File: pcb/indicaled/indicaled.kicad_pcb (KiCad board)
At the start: 2 copper layers, 1 part

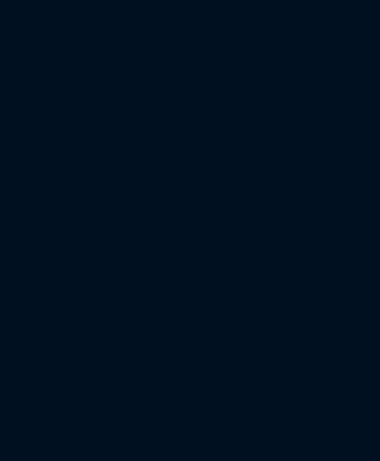
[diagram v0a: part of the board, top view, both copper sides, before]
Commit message: adicionando valores aos componentes
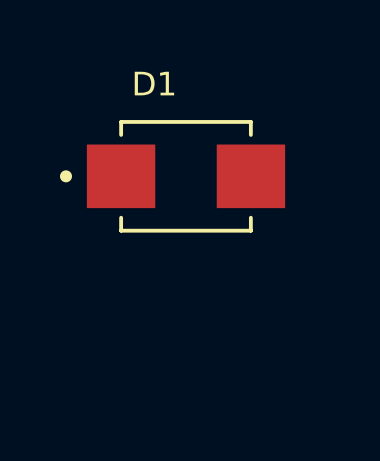
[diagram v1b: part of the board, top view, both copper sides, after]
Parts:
- added D1: D, ss26:SS26, F.Cu at (190.3, 110.2)
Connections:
- U1 pad 1: unconnected-(U1-BOOT-Pad1) -> Net-(U1-BOOT)
- U1 pad 2: unconnected-(U1-VIN-Pad2) -> VIN
- U1 pad 3: unconnected-(U1-EN-Pad3) -> Net-(U1-EN)
- U1 pad 4: unconnected-(U1-SS-Pad4) -> Net-(U1-SS)
- U1 pad 5: unconnected-(U1-VSENSE-Pad5) -> Net-(U1-VSENSE)
- U1 pad 6: unconnected-(U1-COMP-Pad6) -> Net-(U1-COMP)
- U1 pad 7: unconnected-(U1-GND-Pad7) -> GND
- U1 pad 8: unconnected-(U1-PH-Pad8) -> Net-(D1-K)

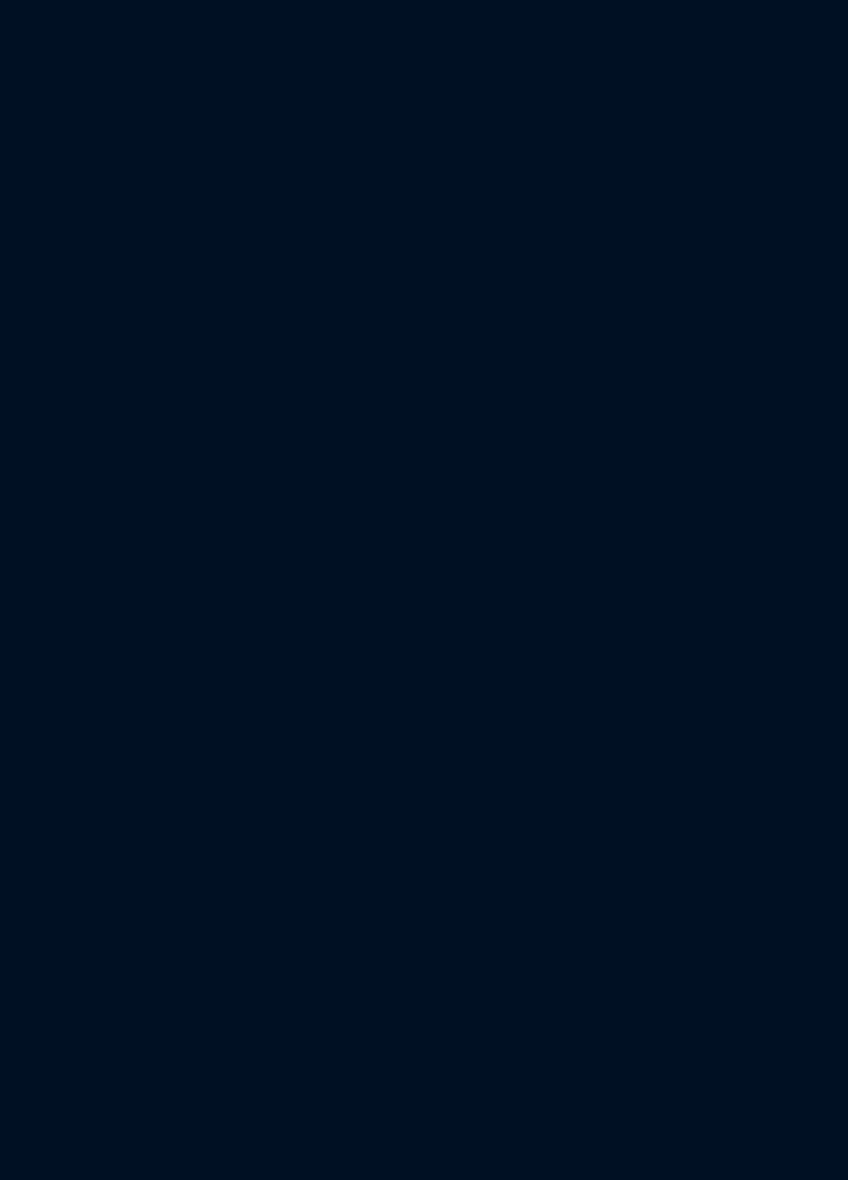
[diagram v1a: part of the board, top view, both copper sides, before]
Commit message: adicionando footprints aos componentes do circuito de alimentação
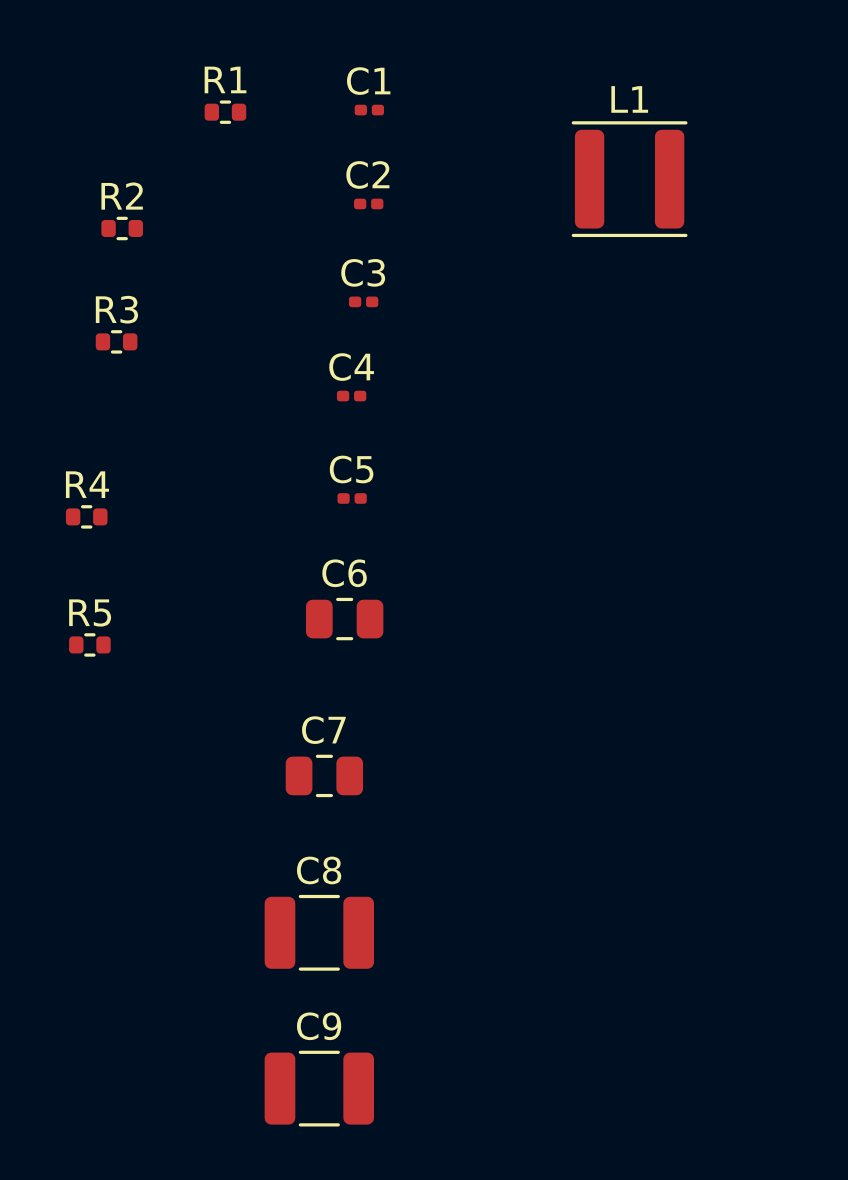
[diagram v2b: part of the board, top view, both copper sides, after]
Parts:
- added C1: 4.7nF, Capacitor_SMD:C_0201_0603Metric, F.Cu at (166.8, 105.1)
- added C2: 39pF, Capacitor_SMD:C_0201_0603Metric, F.Cu at (166.8, 108.6)
- added C3: .01uF, Capacitor_SMD:C_0201_0603Metric, F.Cu at (166.6, 112.3)
- added C4: .1uF, Capacitor_SMD:C_0201_0603Metric, F.Cu at (166.1, 115.8)
- added C5: .01uF, Capacitor_SMD:C_0201_0603Metric, F.Cu at (166.1, 119.7)
- added C6: 4700pF, Capacitor_SMD:C_0805_2012Metric, F.Cu at (165.8, 124.2)
- added C7: 39pF, Capacitor_SMD:C_0805_2012Metric, F.Cu at (165.1, 130.1)
- added C8: 33uF, Capacitor_SMD:C_1210_3225Metric, F.Cu at (164.9, 135.9)
- added C9: 33uF, Capacitor_SMD:C_1210_3225Metric, F.Cu at (164.9, 141.8)
- added L1: 6.8uH, Inductor_SMD:L_APV_ANR4020, F.Cu at (176.5, 107.7)
- added R1: 10k, Resistor_SMD:R_0402_1005Metric, F.Cu at (161.4, 105.2)
- added R2: 1.91k, Resistor_SMD:R_0402_1005Metric, F.Cu at (157.5, 109.5)
- added R3: 49.9k, Resistor_SMD:R_0402_1005Metric, F.Cu at (157.3, 113.8)
- added R4: 10k, Resistor_SMD:R_0402_1005Metric, F.Cu at (156.2, 120.3)
- added R5: 1.9k, Resistor_SMD:R_0402_1005Metric, F.Cu at (156.3, 125.1)

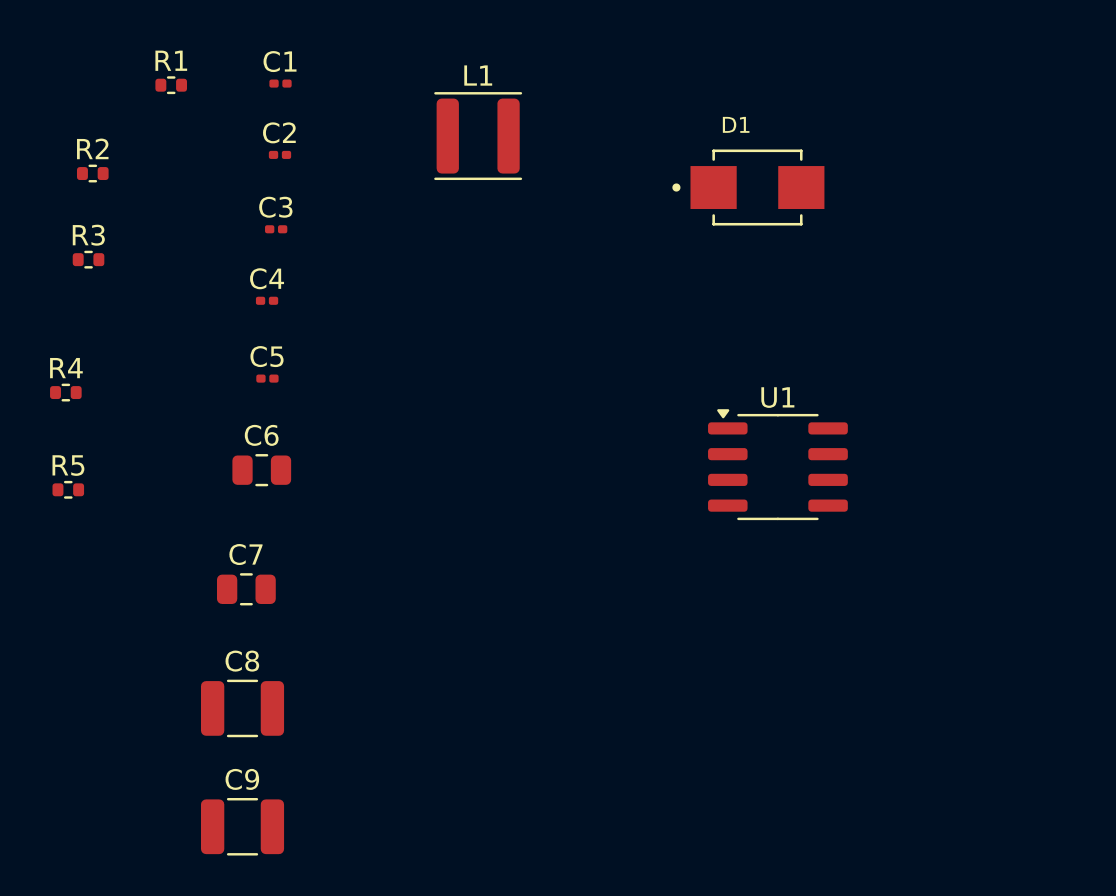
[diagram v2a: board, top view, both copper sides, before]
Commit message: fazendo as ligações do circuito de alimentação e mudando o footprint do D1
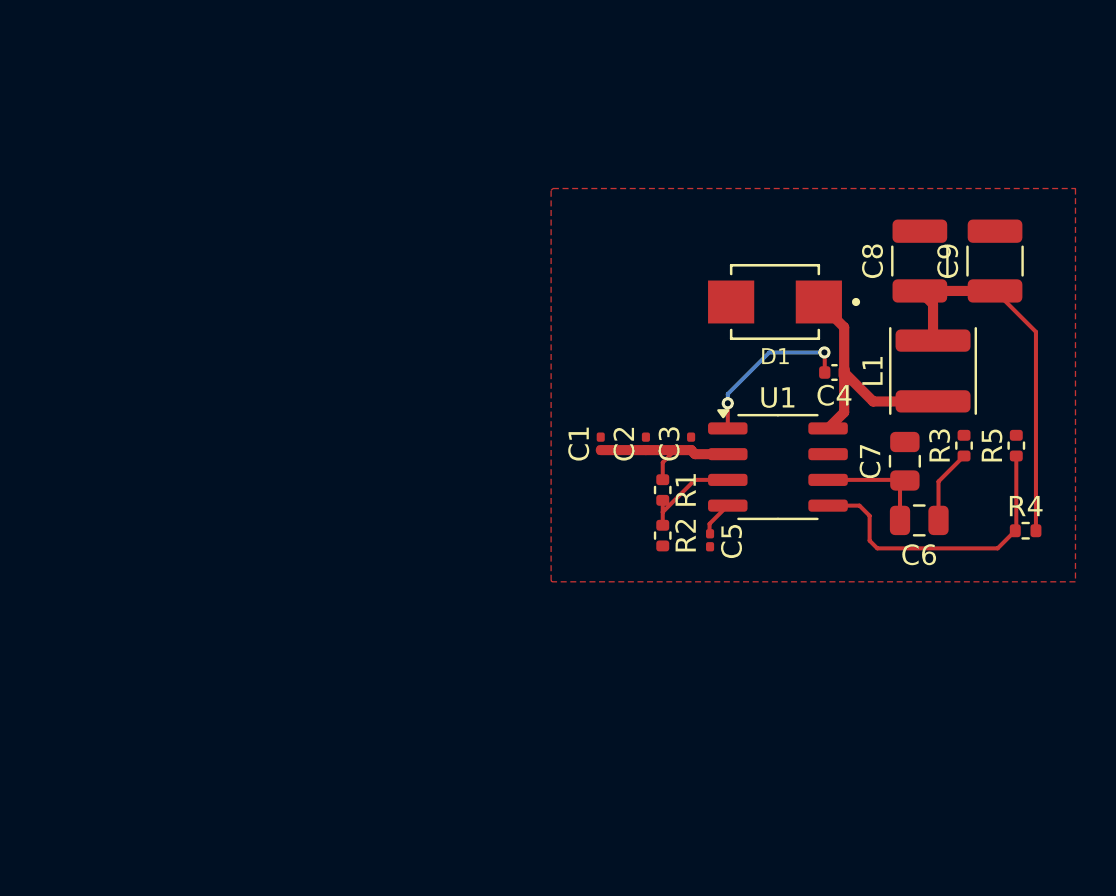
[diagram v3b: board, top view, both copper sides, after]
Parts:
- C4: footprint Capacitor_SMD:C_0201_0603Metric -> Capacitor_SMD:C_0402_1005Metric
- D1: value D -> SS26
- moved R4 47.9 mm to (203.6, 127.2), turned to 180 degrees
- moved R5 46.8 mm to (203.1, 123.0), turned to 90 degrees
- moved C9 46.5 mm to (202.0, 113.8), turned to 90 degrees
- moved R3 44.2 mm to (200.5, 123.0), turned to 90 degrees
- moved C8 40.1 mm to (198.3, 113.8), turned to 90 degrees
- moved R2 33.3 mm to (185.6, 127.4), turned to -90 degrees
- moved C7 33.1 mm to (197.6, 123.7), turned to 90 degrees
- moved C6 32.5 mm to (198.3, 126.7)
- moved R1 31.4 mm to (185.6, 125.2), turned to -90 degrees
- moved C4 28.2 mm to (194.1, 119.3), turned to 180 degrees
- moved L1 25.3 mm to (199.0, 119.3), turned to 90 degrees
- moved C1 23.8 mm to (182.6, 122.9), turned to 90 degrees
- moved C5 23.3 mm to (188.0, 127.6), turned to -90 degrees
- moved C3 23.1 mm to (187.0, 122.9), turned to 90 degrees
- moved C2 23.0 mm to (184.8, 122.9), turned to 90 degrees
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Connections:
- C4 pad 1: Net-(D1-K) -> Net-(U1-PH)
- L1 pad 1: Net-(D1-K) -> Net-(U1-PH)
- U1 pad 8: Net-(D1-K) -> Net-(U1-PH)
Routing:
- net VOUT: track 0.00 -> 19.1 mm
- net Net-(U1-VSENSE): track 0.00 -> 14.9 mm
- net Net-(U1-PH): track 0.00 -> 12.1 mm
- net Net-(U1-BOOT): track 0.00 -> 8.32 mm, vias 0 -> 2
- net VIN: track 0.00 -> 8.07 mm
- net Net-(U1-COMP): track 0.00 -> 5.87 mm
- net Net-(U1-EN): track 0.00 -> 5.10 mm
- net Net-(C6-Pad2): track 0.00 -> 3.70 mm
- net Net-(U1-SS): track 0.00 -> 1.87 mm
- added copper zone on F.Cu, net GND

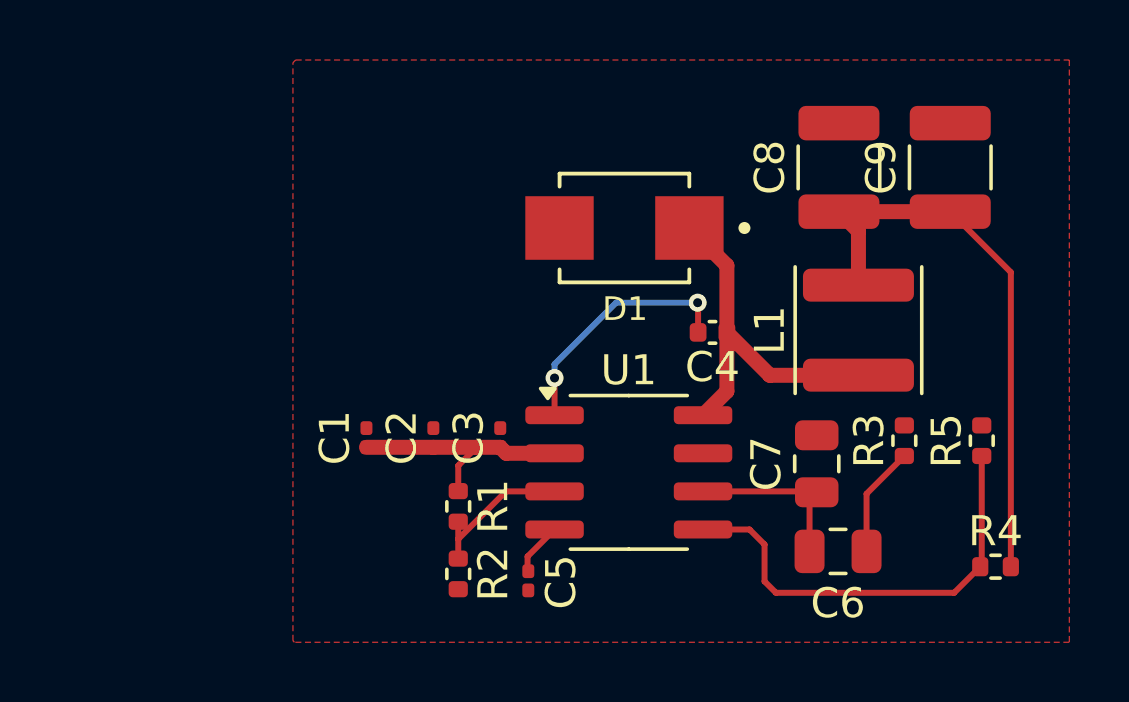
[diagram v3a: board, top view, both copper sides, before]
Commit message: trocando os capacitores de acoplamento de 0201 para 1210
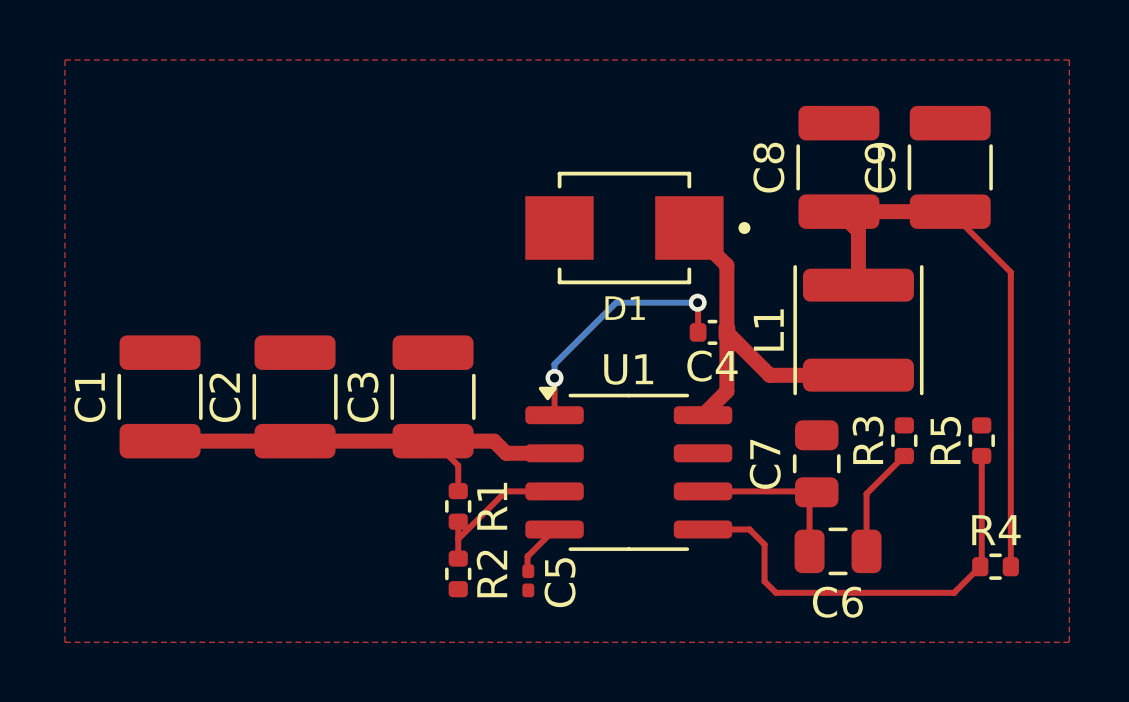
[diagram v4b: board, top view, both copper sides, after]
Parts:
- C1, C2, C3: footprint Capacitor_SMD:C_0201_0603Metric -> Capacitor_SMD:C_1210_3225Metric
- moved C1 7.01 mm to (175.7, 121.5)
- moved C2 4.81 mm to (180.2, 121.5)
- moved C3 2.62 mm to (184.8, 121.5)
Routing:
- net VIN: track 8.07 -> 15.3 mm

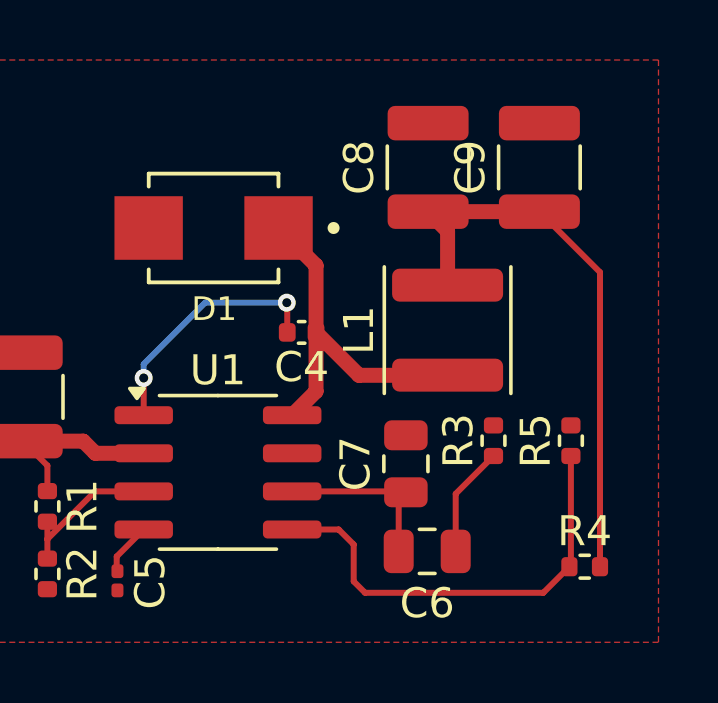
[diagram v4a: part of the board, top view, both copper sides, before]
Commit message: trocando o S26 por S24, adicionando alguns datasheets e reposicionando os componentes na PCB
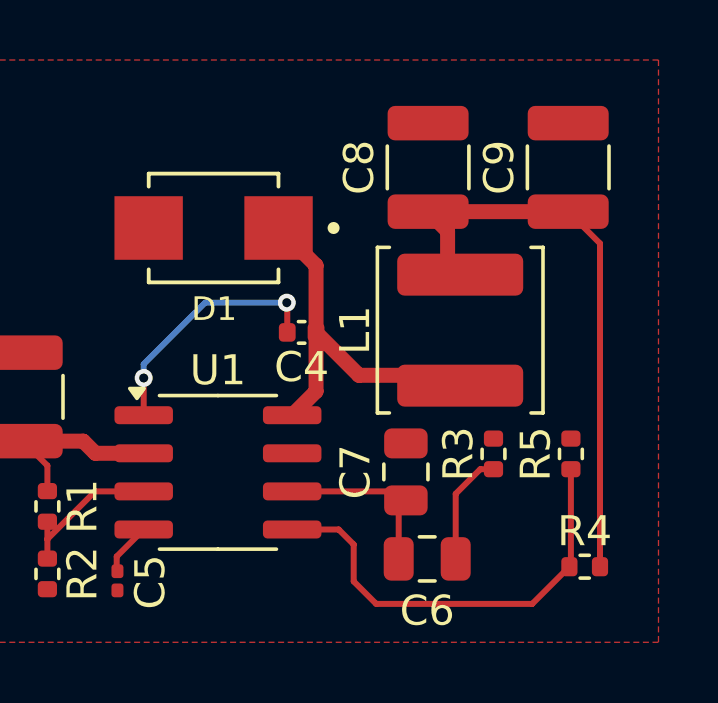
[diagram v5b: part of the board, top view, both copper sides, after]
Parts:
- C3: value .01uF -> 10nF
- C4: value .1uF -> 0.1uF
- C5: value .01uF -> 0.01uF
- D1: value SS26 -> SS24FL
- L1: footprint Inductor_SMD:L_APV_ANR4020 -> Inductor_SMD:L_APV_ANR5040
- moved C9 0.96 mm to (203.0, 113.8)
- moved R3 0.44 mm to (200.5, 123.4)
- moved R5 0.44 mm to (203.1, 123.4)
- moved L1 0.42 mm to (199.4, 119.3)
- moved C7 0.27 mm to (197.6, 124.0)
- moved C6 0.25 mm to (198.3, 126.9)
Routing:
- net VOUT: track 19.1 -> 19.7 mm
- net Net-(U1-COMP): track 5.87 -> 6.42 mm
